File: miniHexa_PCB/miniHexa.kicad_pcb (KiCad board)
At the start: 2 copper layers, 94 x 65.9 mm, 78 parts, among them J2 12v DC, U1 STM32F401RETx, U2 HT7333, U3 RT8289GSP, U4 BQ25886RGE, U5 PCA9685BS, Y1 16Mhz

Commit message: update
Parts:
- removed C2: 20p, Capacitor_SMD:C_0805_2012Metric
- removed U2: HT7333, Package_TO_SOT_SMD:SOT-89-3
- removed Y1: 16Mhz, Crystal:Crystal_HC49-4H_Vertical
- added C26: 100nF, Capacitor_SMD:C_0805_2012Metric, F.Cu at (152.6, 84.4)
- added U6: AMS1117-3.3, Package_TO_SOT_SMD:SOT-223-3_TabPin2, F.Cu at (143.4, 82.5)
- added Y2: 25mhz, Oscillator:Oscillator_SMD_Abracon_ASE-4Pin_3.2x2.5mm, F.Cu at (166.2, 94.6)
- C1: value 20p -> 20uF
- moved U3 53.4 mm to (197.9, 92.7)
- moved C1 32.4 mm to (127.0, 79.0)
- moved C4 32.4 mm to (127.0, 88.0)
- moved C3 32.4 mm to (127.0, 85.0)
- moved C5 32.4 mm to (127.0, 91.0)
- moved C6 32.4 mm to (127.0, 94.0)
- moved C10 32.4 mm to (131.4, 88.0)
- moved C7 32.4 mm to (131.4, 79.0)
- moved C13 32.4 mm to (131.4, 91.0)
- moved C8 32.4 mm to (131.4, 82.0)
- moved C9 32.4 mm to (131.4, 85.0)
- moved L1 1.60 mm to (210.8, 57.2)
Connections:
- C1 pad 2: Net-(U1-PH0) -> Net-(U1-VCAP1)
- U1 pad 30: unconnected-(U1-VCAP1-Pad30) -> Net-(U1-VCAP1)
- U1 pad 6: Net-(U1-PH1) -> unconnected-(U1-PH1-Pad6)
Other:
- copper layers 2 -> 4

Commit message: simple update
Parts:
- C1, C11, C12, C13, C14, C15, C16, C17, C18, C19, C20, C21, C22, C23, C24, C25, C26, C3, C4, C5, C6, C7, C8, C9: footprint Capacitor_SMD:C_0805_2012Metric -> Capacitor_SMD:C_0402_1005Metric
- C10: value 1u -> 1uF; footprint Capacitor_SMD:C_0805_2012Metric -> Capacitor_SMD:C_0402_1005Metric
- J2: moved to B.Cu
- L1, L2: footprint Inductor_SMD:L_APV_APH0850 -> Inductor_SMD:L_Panasonic_PCC-M0850M
- moved BT1 205.0 mm to (60.2, 58.2), turned to 0 degrees
- moved C11 67.0 mm to (227.6, 78.6)
- moved C12 67.0 mm to (227.6, 81.6)
- moved D2 67.0 mm to (230.6, 72.2)
- moved R22 67.0 mm to (230.5, 75.2)
- moved C26 25.4 mm to (127.3, 81.4)
- moved L2 2.20 mm to (185.8, 81.7)
- moved Servo18 2.20 mm to (190.0, 100.6)
- moved Servo17 1.40 mm to (190.0, 107.6)
- moved J2 0.78 mm to (207.7, 81.7), turned to 90 degrees
- moved Servo16 0.60 mm to (190.0, 114.6)
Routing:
- net GND: track 0.00 -> 42.1 mm
- net +5V: track 0.00 -> 42.0 mm
- net (no net): track 0.00 -> 1.05 mm

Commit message: layout phase pcb
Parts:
- removed MK-L1: INMP441-L, Audio_Module:MIC_INMP441ACEZ-R7
- removed MK-R1: INMP441-R, Audio_Module:MIC_INMP441ACEZ-R7
- removed R13, R14, R15, R16, R17, R18: 1k, Resistor_SMD:R_0805_2012Metric
- removed R29: 100k, Resistor_SMD:R_0805_2012Metric
- added C30: 100nF, Capacitor_SMD:C_0402_1005Metric, F.Cu at (163.5, 132.0)
- added C31: 100nF, Capacitor_SMD:C_0402_1005Metric, F.Cu at (163.5, 135.0)
- added MK1: ICS-R, Sensor_Audio:InvenSense_ICS-43434-6_3.5x2.65mm, F.Cu at (166.3, 66.5)
- added MK2: ICS - L, Sensor_Audio:InvenSense_ICS-43434-6_3.5x2.65mm, F.Cu at (167.0, 103.7)
- added R1: 10k, Resistor_SMD:R_0402_1005Metric, F.Cu at (177.3, 94.1)
- added R32: 100k, Resistor_SMD:R_0402_1005Metric, F.Cu at (168.0, 132.0)
- added SW1: SW_Push, Button_Switch_SMD:SW_SPST_B3U-1000P, F.Cu at (173.5, 96.1)
- C11, C12, C14, C15, C16, C17, C18, C20, C21, C23, D3, D4, D5, L1, L2, U3, U4, U6: moved to B.Cu
- C19: footprint Capacitor_SMD:C_0402_1005Metric -> Capacitor_SMD:CP_Elec_6.3x7.7; moved to B.Cu
- C22: value C -> 10uF; moved to B.Cu
- C24: value C -> 47nF; moved to B.Cu
- C25: value C -> 4.7uF; moved to B.Cu
- C8: value 10n -> 10nF
- C9: value 1u -> 1uF
- R20, R21, R22: footprint Resistor_SMD:R_0805_2012Metric -> Resistor_SMD:R_0402_1005Metric
- R23, R24, R25, R26, R30, R31: footprint Resistor_SMD:R_0805_2012Metric -> Resistor_SMD:R_0402_1005Metric; moved to B.Cu
- R27, R28: value R -> 2.2k; footprint Resistor_SMD:R_0805_2012Metric -> Resistor_SMD:R_0402_1005Metric; moved to B.Cu
- U5: moved to F.Cu
- moved R24 87.8 mm to (171.0, 89.6), turned to 90 degrees
- moved R25 83.9 mm to (171.0, 86.2), turned to 90 degrees
- moved C19 83.8 mm to (162.8, 89.5), turned to 90 degrees
- moved C18 80.9 mm to (168.2, 89.5), turned to -90 degrees
- moved C17 80.7 mm to (168.2, 86.3), turned to -90 degrees
- moved C12 68.8 mm to (159.3, 72.7), turned to 180 degrees
- moved C14 68.7 mm to (185.0, 78.5), turned to 180 degrees
- moved C11 67.9 mm to (159.6, 79.7)
- moved R27 66.8 mm to (194.6, 82.7), turned to 180 degrees
- moved D4 64.6 mm to (197.1, 81.8), turned to -90 degrees
- moved R26 63.3 mm to (192.2, 77.2)
- moved R23 62.0 mm to (193.0, 72.5), turned to 180 degrees
- moved R30 61.0 mm to (195.0, 80.5), turned to 180 degrees
- moved R28 59.9 mm to (187.5, 82.5), turned to -90 degrees
- moved C15 59.5 mm to (191.0, 74.5), turned to 90 degrees
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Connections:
- C25 pad 1: Net-(U4-REGN) -> GND
- C25 pad 2: GND -> Net-(U4-REGN)
- Servo13 pad 3: Net-(Servo13-Pin_3) -> SERVO13
- Servo14 pad 3: Net-(Servo14-Pin_3) -> SERVO14
- Servo15 pad 3: Net-(Servo15-Pin_3) -> SERVO15
- Servo16 pad 3: Net-(Servo16-Pin_3) -> SERVO16
- Servo17 pad 3: Net-(Servo17-Pin_3) -> SERVO17
- Servo18 pad 3: Net-(Servo18-Pin_3) -> SERVO18
- U4 pad 5: unconnected-(U4-OTG-Pad5) -> GND
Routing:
- net +5V: track 42.0 -> 102.9 mm
- net GND: track 42.1 -> 96.2 mm
- net FB: track 0.00 -> 24.1 mm
- net Net-(C24-Pad1): track 0.00 -> 15.2 mm
- net Net-(C23-Pad2): track 0.00 -> 14.6 mm
- net VIN: track 0.00 -> 12.9 mm
- net Net-(D3-K): track 0.00 -> 12.1 mm
- net Net-(U4-VBUS): track 0.00 -> 10.6 mm
- net +3.3V: track 0.00 -> 10.5 mm
- net I2C_SDA: track 0.00 -> 5.70 mm
- net Net-(U1-PH0): track 0.00 -> 4.16 mm
- net Net-(U3-BOOT): track 0.00 -> 2.97 mm
- net (no net): track 1.05 -> 0.00 mm
- added copper zone on In1.Cu, net GND

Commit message: layout done
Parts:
- added R2: 0, Resistor_SMD:R_0402_1005Metric, F.Cu at (158.7, 85.2)
- D2, R22: moved to B.Cu
- R19: footprint Resistor_SMD:R_0805_2012Metric -> Resistor_SMD:R_0402_1005Metric
- R21: value R -> 10k
- moved C30 64.8 mm to (170.4, 67.6), turned to 180 degrees
- moved R22 60.2 mm to (175.3, 99.1), turned to -90 degrees
- moved D2 60.1 mm to (175.4, 96.2), turned to 90 degrees
- moved R32 50.1 mm to (158.6, 82.7), turned to 180 degrees
- moved C31 31.2 mm to (170.7, 104.6), turned to 180 degrees
- moved C12 25.8 mm to (175.1, 93.0), turned to 90 degrees
- moved U6 20.7 mm to (170.2, 96.5)
- moved C11 20.6 mm to (165.4, 99.4), turned to 90 degrees
- moved BT1 12.2 mm to (57.9, 46.2)
- moved C19 2.86 mm to (159.9, 89.3)
- moved R20 2.70 mm to (156.6, 84.6)
- moved C17 2.26 mm to (166.6, 87.8)
- moved C18 1.76 mm to (167.9, 87.8)
- moved MK2 1.07 mm to (166.0, 103.9)
- moved U5 0.70 mm to (152.4, 84.5)
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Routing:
- net GND: track 96.2 -> 17.2 mm
- net +5V: track 102.9 -> 42.9 mm, vias 0 -> 1
- net +3.3V: track 10.5 -> 25.2 mm, vias 0 -> 1
- net I2C_SCK: track 0.00 -> 6.73 mm
- net Net-(D2-K): track 0.00 -> 1.50 mm
- net I2C_SDA: track 5.70 -> 6.40 mm
- added copper zone on In2.Cu, net +5V

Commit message: before auto routing
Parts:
- added C2: 22uF, Capacitor_SMD:C_0402_1005Metric, B.Cu at (200.3, 77.1)
- added C27: 100nF, Capacitor_SMD:C_0402_1005Metric, B.Cu at (201.9, 77.1)
- BT1: footprint Battery:BatteryHolder_Keystone_2468_2xAAA -> Connector_JST:JST_XH_S2B-XH-A-1_1x02_P2.50mm_Horizontal
- C23: value C -> 10uF
- moved BT1 156.2 mm to (206.4, 94.3), turned to -90 degrees
- moved C1 48.1 mm to (175.0, 81.7), turned to 180 degrees
- moved R21 10.2 mm to (153.7, 90.7), turned to 90 degrees
- moved R1 2.21 mm to (175.2, 93.4)
- moved C24 1.21 mm to (196.4, 69.5), turned to -135 degrees
- moved C22 1.03 mm to (194.7, 73.8)
- moved C3 0.89 mm to (162.8, 91.7), turned to 180 degrees
- moved C30 0.88 mm to (169.5, 67.5)
- moved C13 0.85 mm to (169.6, 93.8), turned to 45 degrees
- moved C6 0.75 mm to (162.4, 78.2)
- moved C5 0.61 mm to (173.2, 79.8)
- moved C4 0.27 mm to (174.9, 86.7)
- moved C25 0.20 mm to (192.2, 76.0)
- moved R26 0.20 mm to (192.2, 77.0)
- moved C7 0.11 mm to (177.0, 86.7)
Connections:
- Y2 pad 1: Net-(Y2-EN) -> +3.3V
- Y2 pad 4: Net-(Y2-EN) -> +3.3V
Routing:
- net +3.3V: track 25.2 -> 129.0 mm, vias 1 -> 2
- net GND: track 17.2 -> 106.2 mm, vias 0 -> 13
- net Net-(BT1-+): track 0.00 -> 28.9 mm, vias 0 -> 1
- net +5V: track 42.9 -> 56.7 mm, vias 1 -> 2
- net Net-(U1-NRST): track 0.00 -> 8.61 mm
- net Net-(U4-BTST): track 0.00 -> 7.53 mm, vias 0 -> 2
- net Net-(D5-K): track 0.04 -> 5.62 mm
- net Net-(U3-EN): track 0.00 -> 4.89 mm
- net Net-(D5-A): track 0.23 -> 3.05 mm
- net PCA_OE: track 0.00 -> 2.82 mm
- net Net-(U4-ILIM): track 0.00 -> 2.39 mm
- net MIC_SD: track 0.00 -> 2.28 mm
- net Net-(R1-Pad1): track 0.00 -> 2.19 mm
- net Net-(D4-K): track 0.00 -> 2.02 mm
- net Net-(D4-A): track 0.00 -> 2.02 mm
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
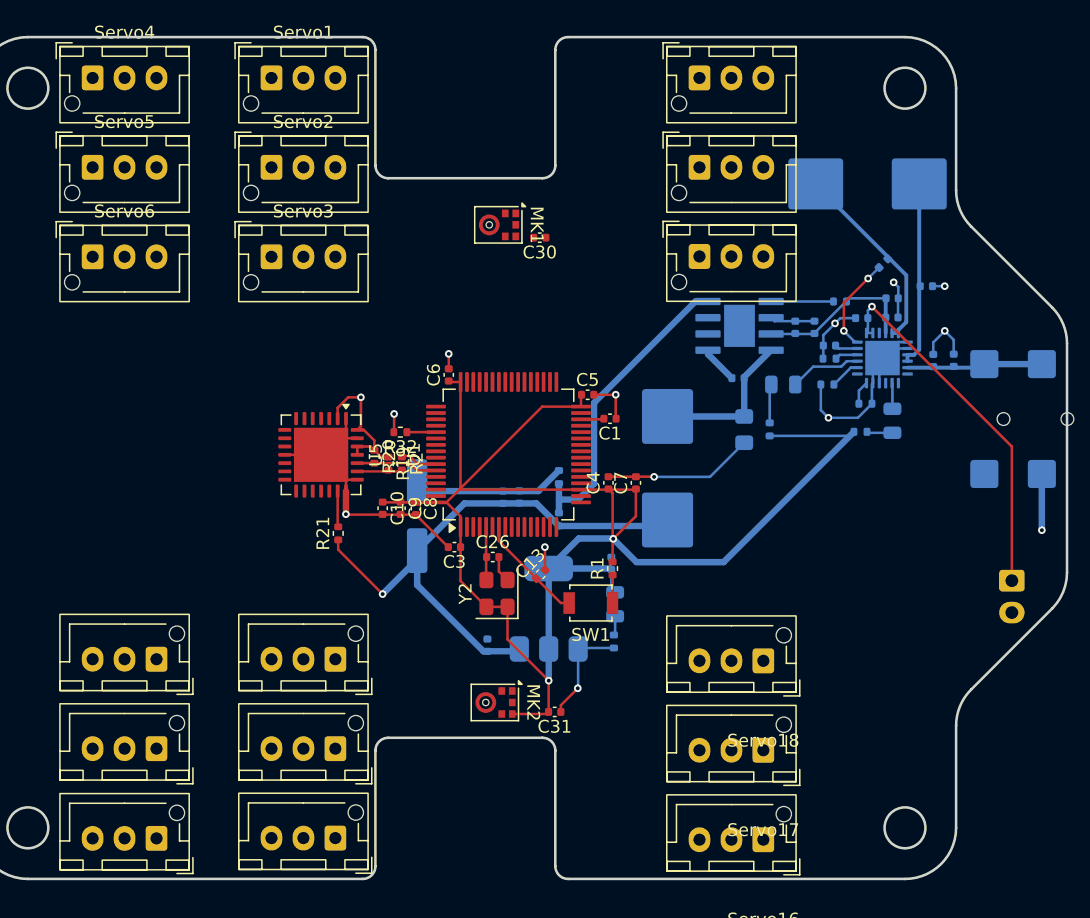
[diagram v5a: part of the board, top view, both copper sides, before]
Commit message: Decided to manually route, looks good
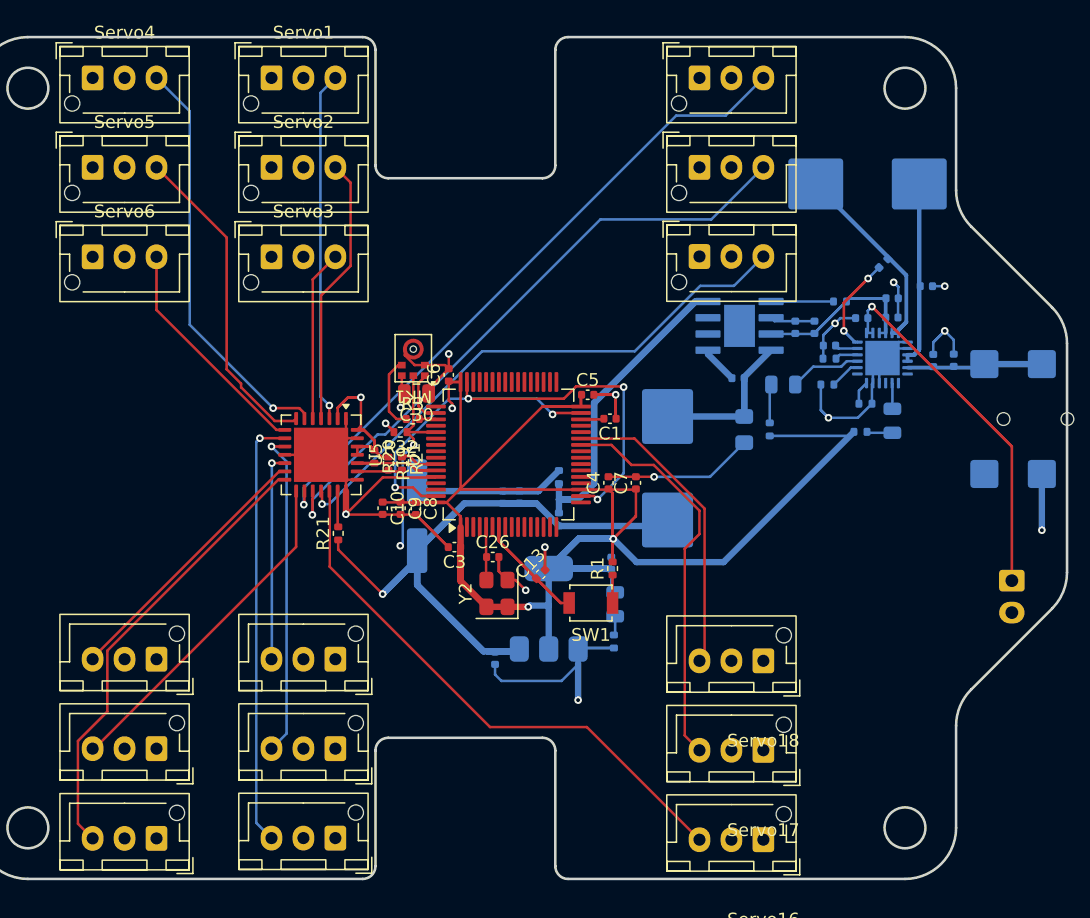
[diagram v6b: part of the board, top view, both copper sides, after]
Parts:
- removed C31: 100nF, Capacitor_SMD:C_0402_1005Metric
- removed MK2: ICS - L, Sensor_Audio:InvenSense_ICS-43434-6_3.5x2.65mm
- added R3: 0, Resistor_SMD:R_0402_1005Metric, F.Cu at (159.6, 81.7)
- C30: footprint Capacitor_SMD:C_0402_1005Metric -> Capacitor_SMD:C_0805_2012Metric
- moved C30 15.6 mm to (159.8, 79.7)
- moved MK1 12.4 mm to (159.6, 76.9), turned to 180 degrees
- moved C11 1.18 mm to (166.0, 100.4), turned to -90 degrees
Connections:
- MK1 pad 2: +3.3V -> GND
- U1 pad 20: MIC_WS -> unconnected-(U1-PA4-Pad20)
- U1 pad 50: unconnected-(U1-PA15-Pad50) -> MIC_WS
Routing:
- net SERVO13: track 0.00 -> 51.7 mm, vias 0 -> 1
- net SERVO14: track 0.00 -> 49.1 mm, vias 0 -> 1
- net GND: track 106.2 -> 154.6 mm, vias 13 -> 14
- net Net-(U1-VSS-Pad18): track 0.00 -> 48.0 mm, vias 0 -> 5
- net SERVO16: track 0.00 -> 43.7 mm
- net SERVO15: track 0.00 -> 43.6 mm, vias 0 -> 1
- net SERVO11: track 0.00 -> 35.6 mm
- net SERVO7: track 0.00 -> 33.9 mm, vias 0 -> 1
- net SERVO4: track 0.00 -> 32.7 mm, vias 0 -> 1
- net +5V: track 56.7 -> 88.3 mm
- net SERVO17: track 0.00 -> 31.1 mm
- net Net-(C23-Pad2): track 14.6 -> 42.1 mm
- net SERVO1: track 0.00 -> 27.4 mm, vias 0 -> 1
- net SERVO12: track 0.00 -> 26.8 mm
- net SERVO8: track 0.00 -> 25.7 mm, vias 0 -> 1
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- added copper zone on In2.Cu, net +3.3V

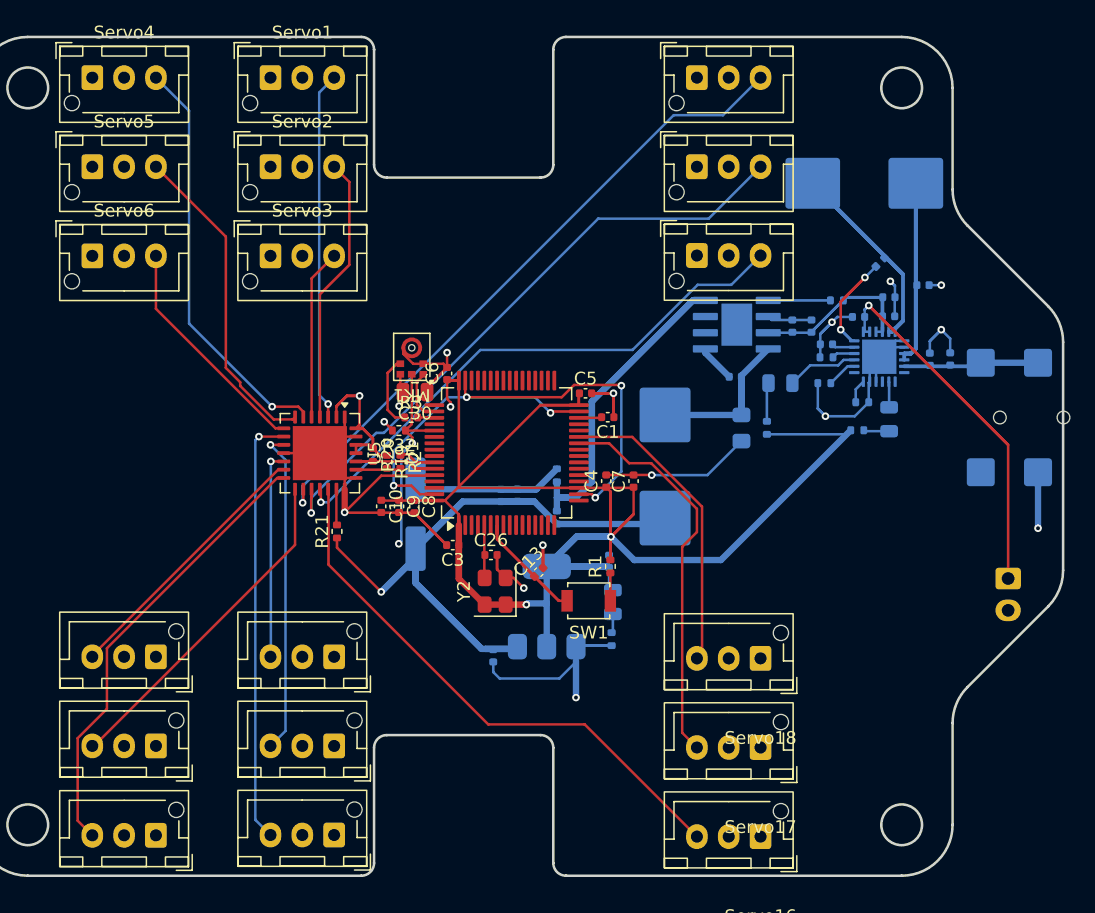
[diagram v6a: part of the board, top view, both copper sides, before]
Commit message: routing complete with drc
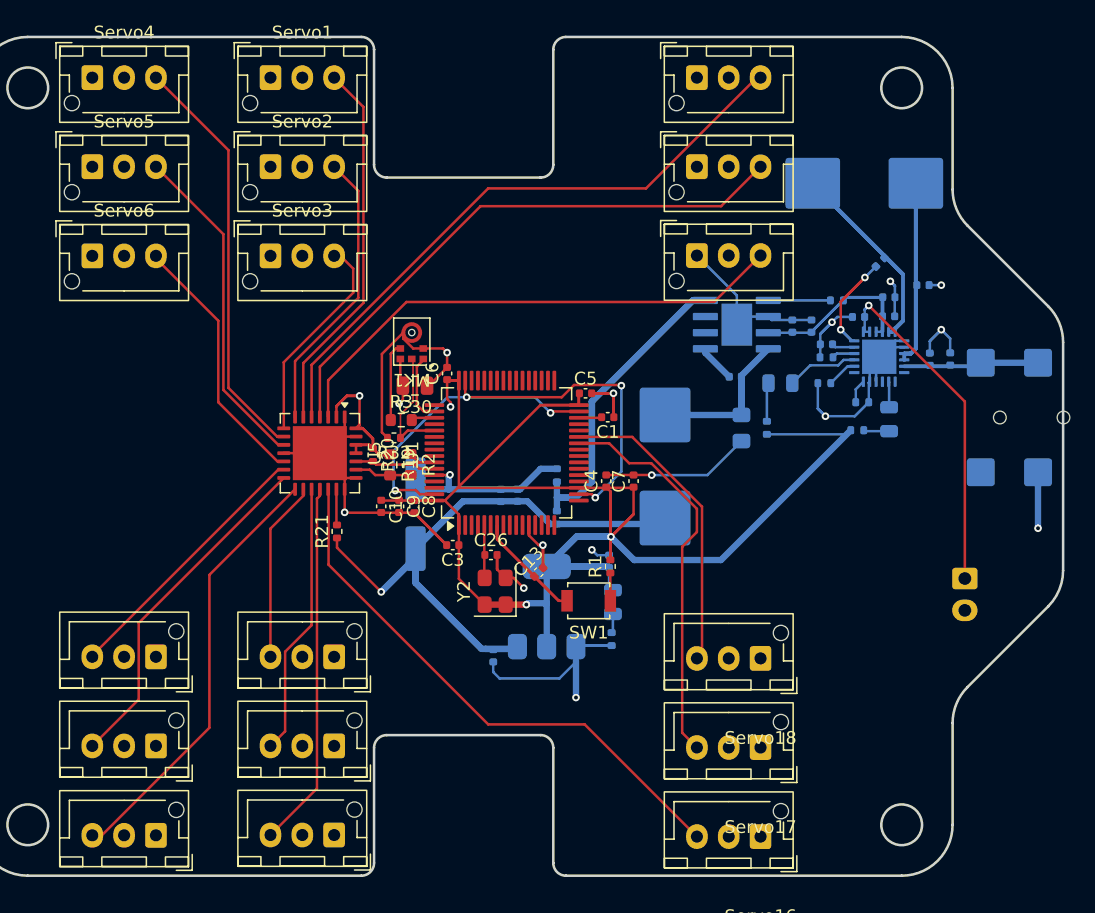
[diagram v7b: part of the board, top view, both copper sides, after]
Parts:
- R19, R2, R3: footprint Resistor_SMD:R_0402_1005Metric -> Resistor_SMD:R_0603_1608Metric
- moved BT1 3.40 mm to (203.1, 94.3)
- moved MK1 1.20 mm to (159.6, 75.7)
- moved R2 0.82 mm to (159.5, 85.4)
- moved R3 0.81 mm to (158.8, 81.9)
- moved R32 0.69 mm to (158.2, 83.3)
- moved C30 0.50 mm to (159.8, 79.2)
- moved R19 0.34 mm to (157.9, 85.4)
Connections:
- U1 pad 12: unconnected-(U1-VSSA-Pad12) -> GND
- U1 pad 18: Net-(U1-VSS-Pad18) -> GND
- U1 pad 31: Net-(U1-VSS-Pad18) -> GND
- U1 pad 47: Net-(U1-VSS-Pad18) -> GND
- U1 pad 63: Net-(U1-VSS-Pad18) -> GND
- U5 pad 10: SERVO8 -> SERVO5
- U5 pad 12: SERVO9 -> SERVO6
- U5 pad 14: SERVO11 -> SERVO12
- U5 pad 15: SERVO12 -> SERVO11
- U5 pad 16: SERVO13 -> SERVO9
- U5 pad 17: SERVO14 -> SERVO8
- U5 pad 18: SERVO15 -> SERVO7
- U5 pad 3: SERVO1 -> SERVO15
- U5 pad 4: SERVO2 -> SERVO14
- U5 pad 5: SERVO3 -> SERVO13
- U5 pad 6: SERVO4 -> SERVO1
- U5 pad 7: SERVO5 -> SERVO2
- U5 pad 8: SERVO6 -> SERVO3
- U5 pad 9: SERVO7 -> SERVO4
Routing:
- net GND: track 154.6 -> 215.5 mm, vias 14 -> 20
- net Net-(U1-VSS-Pad18): track 48.0 -> 0.00 mm, vias 5 -> 0
- net Net-(BT1-+): track 44.9 -> 28.0 mm
- net MIC_SD: track 16.5 -> 9.55 mm, vias 2 -> 0
- net SERVO7: track 33.9 -> 28.8 mm, vias 1 -> 0
- net SERVO8: track 25.7 -> 21.5 mm, vias 1 -> 0
- net SERVO14: track 49.1 -> 45.1 mm, vias 1 -> 0
- net I2C_SDA: track 10.0 -> 6.40 mm
- net SERVO3: track 13.4 -> 16.7 mm
- net SERVO13: track 51.7 -> 48.7 mm, vias 1 -> 0
- net SERVO15: track 43.6 -> 40.9 mm, vias 1 -> 0
- net +5V: track 88.3 -> 85.7 mm
- net SERVO6: track 18.1 -> 20.6 mm
- net SERVO9: track 16.4 -> 14.2 mm, vias 1 -> 0
- net SERVO1: track 27.4 -> 29.6 mm, vias 1 -> 0
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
